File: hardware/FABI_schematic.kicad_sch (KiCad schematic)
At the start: 58 parts, among them J1 Conn_01x04_Male, J1 Conn_ARM_SWD_TagConnect_TC2030, J11_GND1 Conn_01x01_Male, J11_VDD1 Conn_01x01_Male, J11_data1 Conn_01x01_Male, J12 Conn_01x04_Socket, J2 display_connector_91601-304LF, J3 54601-906WPLF, J4 54-00174 / FC68125, J5 54-00174 / FC68125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

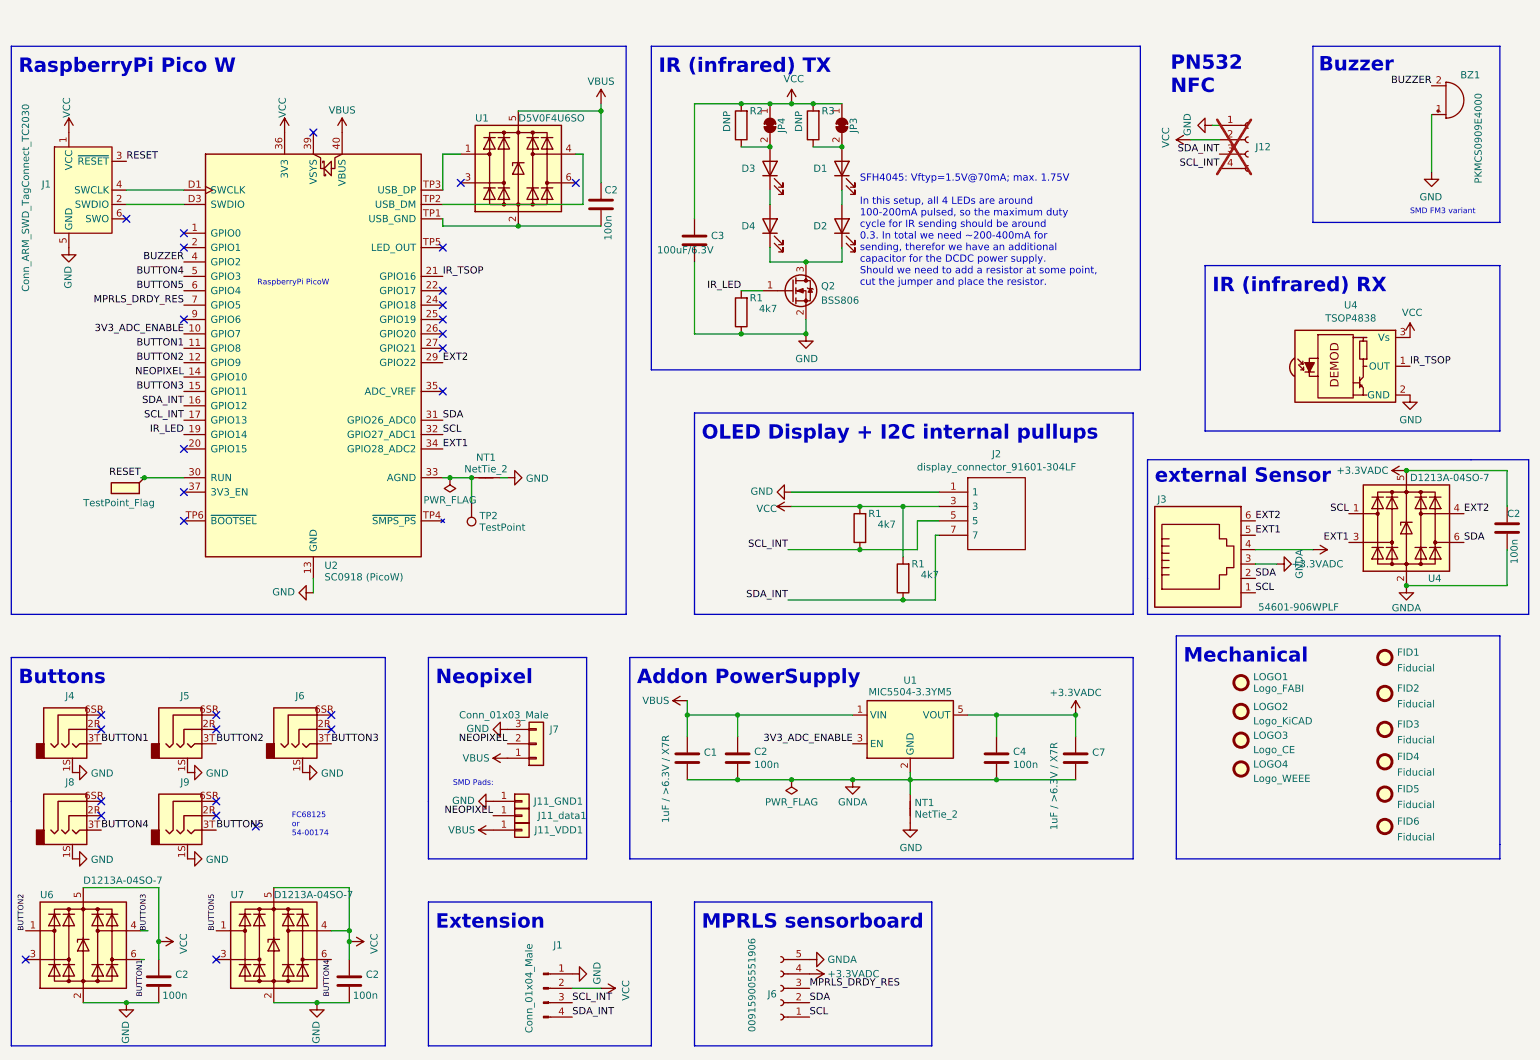
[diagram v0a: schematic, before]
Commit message: First Version BMS; Redundant Components removed; Rewired VCC components as preparation for low power design
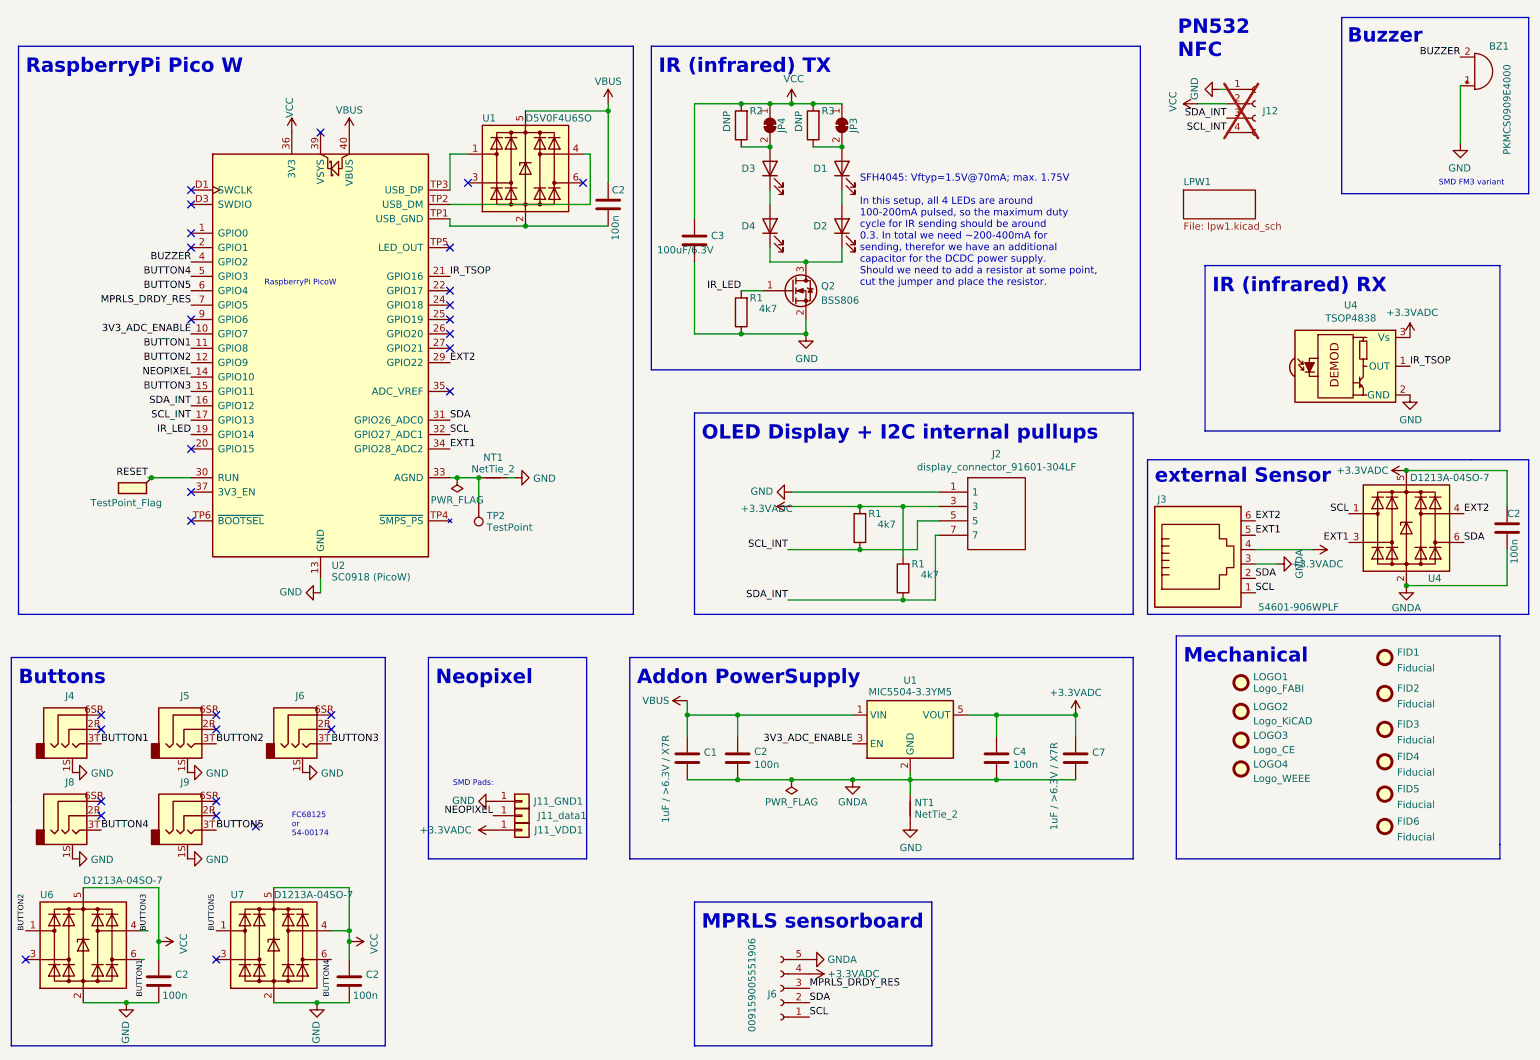
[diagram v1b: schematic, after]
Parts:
- removed J1: Conn_ARM_SWD_TagConnect_TC2030, Connector:Tag-Connect_TC2030-IDC-FP_2x03_P1.27mm_Vertical, symbol Connector:Conn_ARM_SWD_TagConnect_TC2030
- removed J1: Conn_01x04_Male, FLipMouse:pressure_sensor, symbol Connector:Conn_01x04_Pin
- removed J7: Conn_01x03_Male, Connector_PinHeader_2.54mm:PinHeader_1x03_P2.54mm_Vertical, symbol Connector_Generic:Conn_01x03
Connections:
- net +3.3VADC: now also J11_VDD1.1 (Pin_1), J2.3, R1.2, R1.2, U4.3 (Vs)
- net VBUS: no longer J11_VDD1.1 (Pin_1)
- net VCC: no longer J2.3, R1.2, R1.2, U4.3 (Vs)
- no-connect marks 30 -> 31
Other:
- added sheet LPW1 (lpw1.kicad_sch)
- note removed: "Extension"
- moved on the sheet: BZ1, C2, J12, NT1, TP2, U1, U2
